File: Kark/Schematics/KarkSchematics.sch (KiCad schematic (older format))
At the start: 29 parts

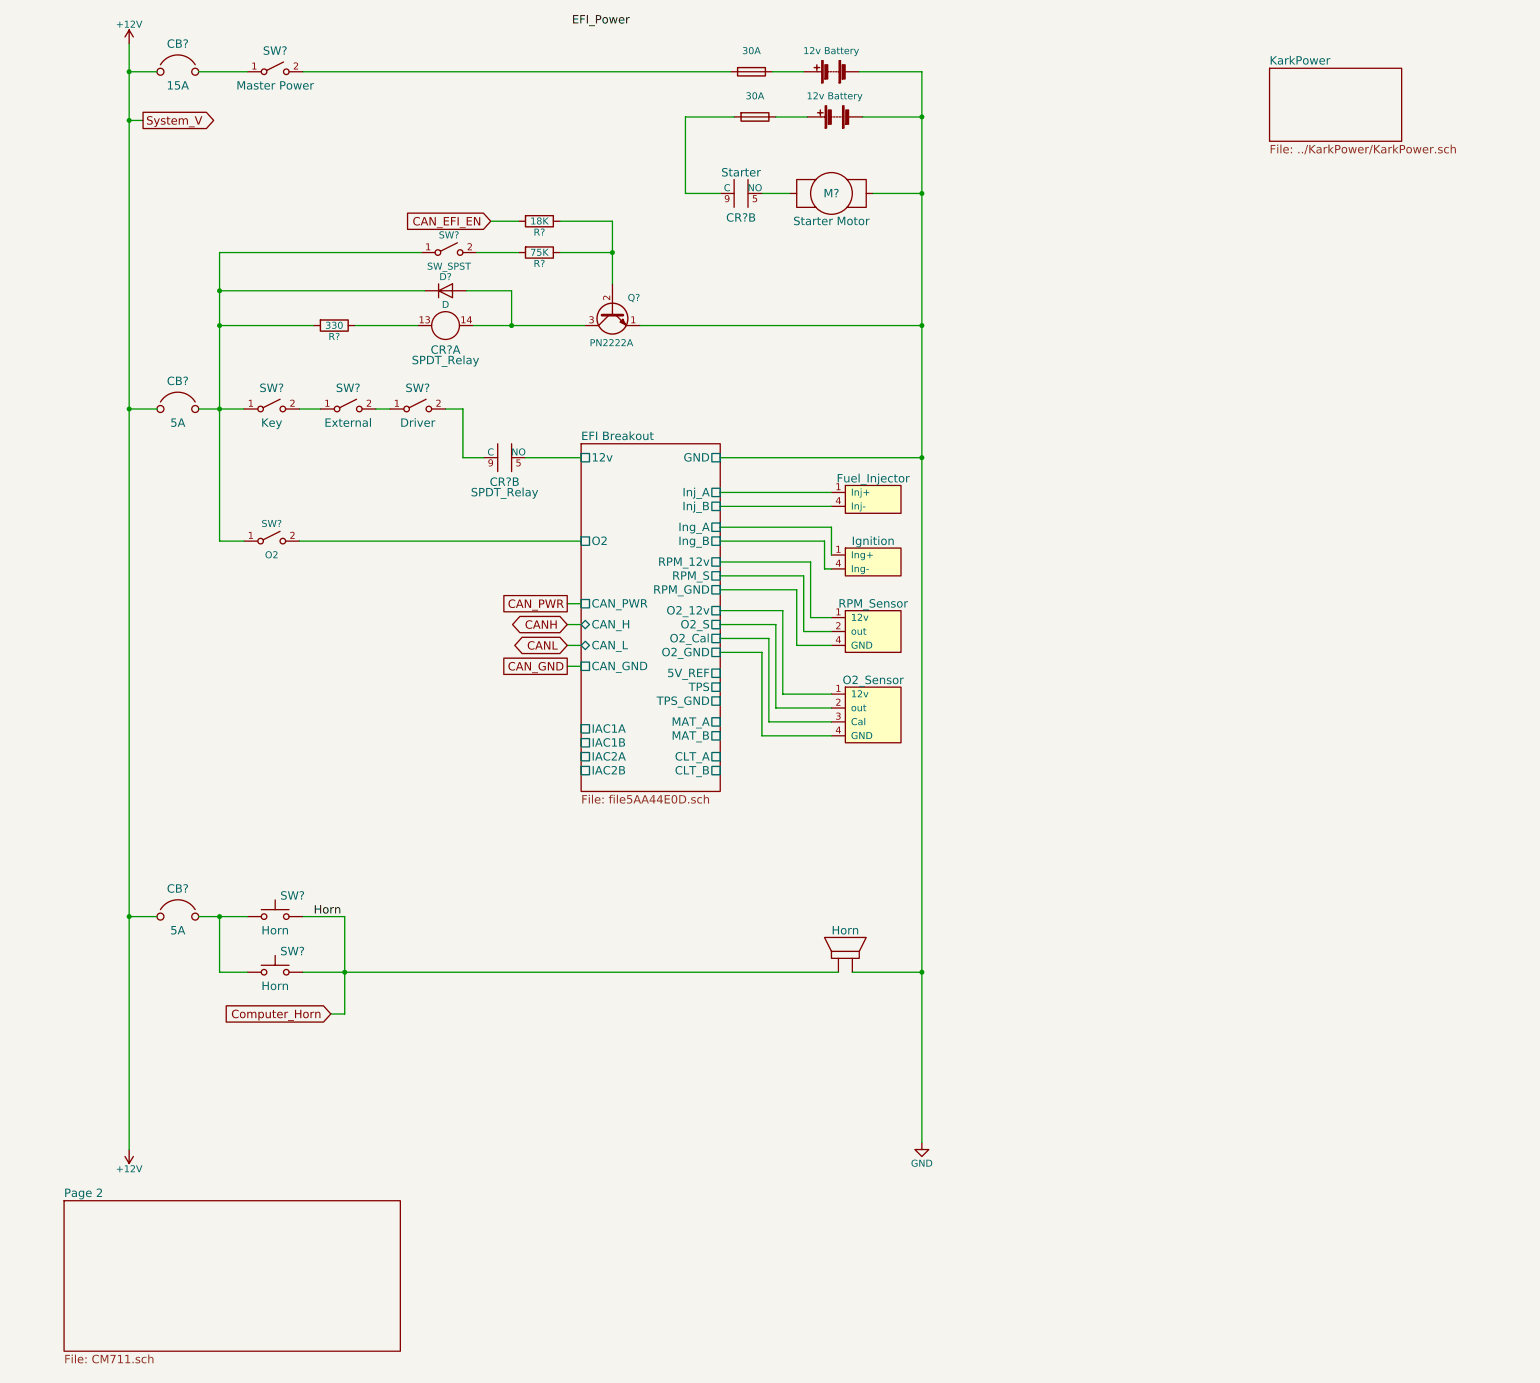
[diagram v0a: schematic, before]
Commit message: Added Starter and Fuel pump
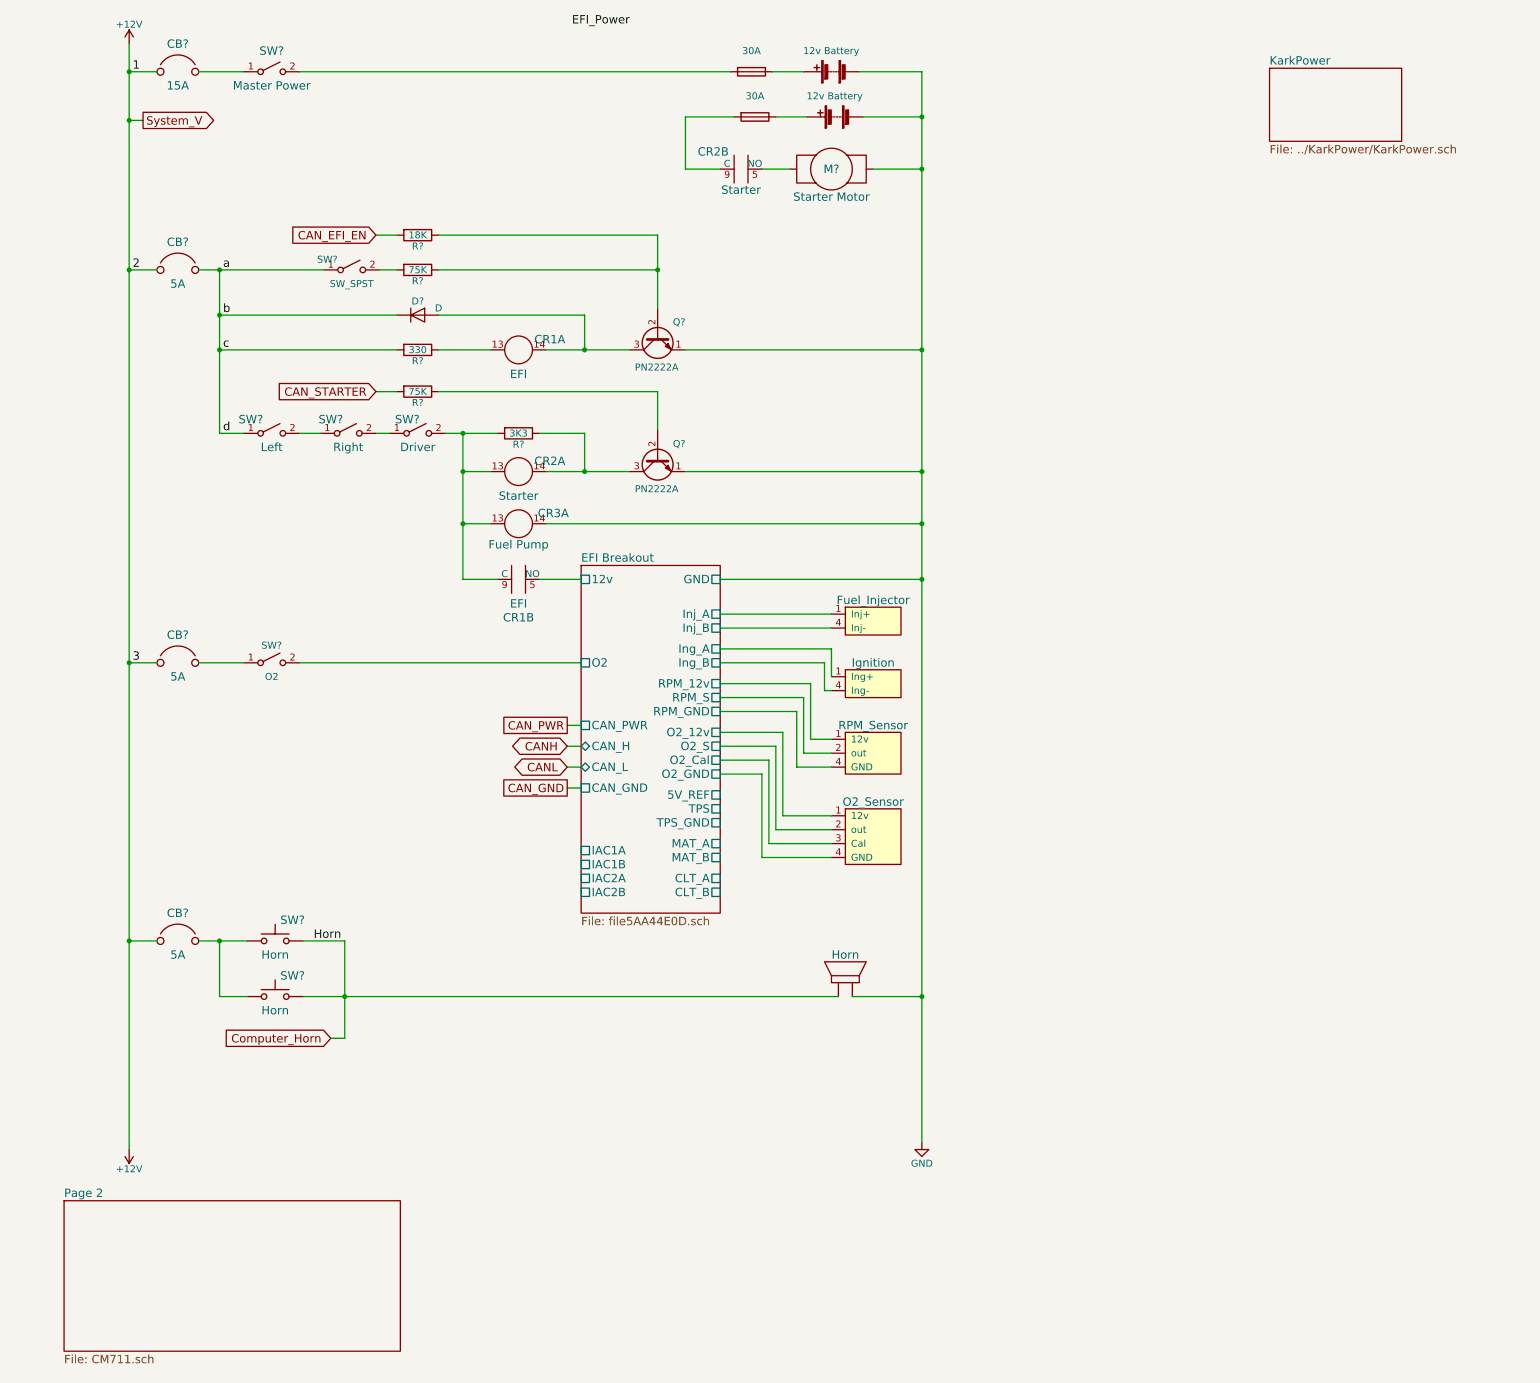
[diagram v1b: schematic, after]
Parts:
- added CB?: 5A, symbol CB
- added unit 1 of CR2
- added CR3: Fuel Pump, symbol SPDT_Relay
- added Q?: PN2222A, TO_SOT_Packages_THT:TO-92_Inline_Wide, symbol PN2222A
- added R?: 75K, Resistors_THT:R_Axial_DIN0207_L6.3mm_D2.5mm_P7.62mm_Horizontal, symbol R
- added R?: 3K3, Resistors_THT:R_Axial_DIN0207_L6.3mm_D2.5mm_P7.62mm_Horizontal, symbol R
- CR1: renamed from CR?; value SPDT_Relay -> EFI
- SW?: value Key -> Left
- SW?: value External -> Right
- gave numbers to parts that had none: 1
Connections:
- net +12V: now also CB?.1 (Line)
- net GND: now also CR3.14, Q?.1 (E)
- net a: now reaches CB?.2 (Load), D?.1 (K), R?.2, SW?.1 (A), SW?.1 (A)
- net a: no longer SW?.1 (A)
- net at CR1.9 (C), SW?.2 (B): now also CR2.13, CR3.13, R?.2
- new net: CB?.2 (Load), SW?.1 (A)
- new net: Q?.2 (B), R?.1
- new net: CR2.14, Q?.3 (C), R?.1
- new net CAN_STARTER: R?.2
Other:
- moved on the sheet: CB?, CR1A, CR1B, CR2B, D?, M?, Q?, R?, SW?

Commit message: Schematic corrections
Corrected wiring for fuel pump and moved the EFI chip over to accomodate the change
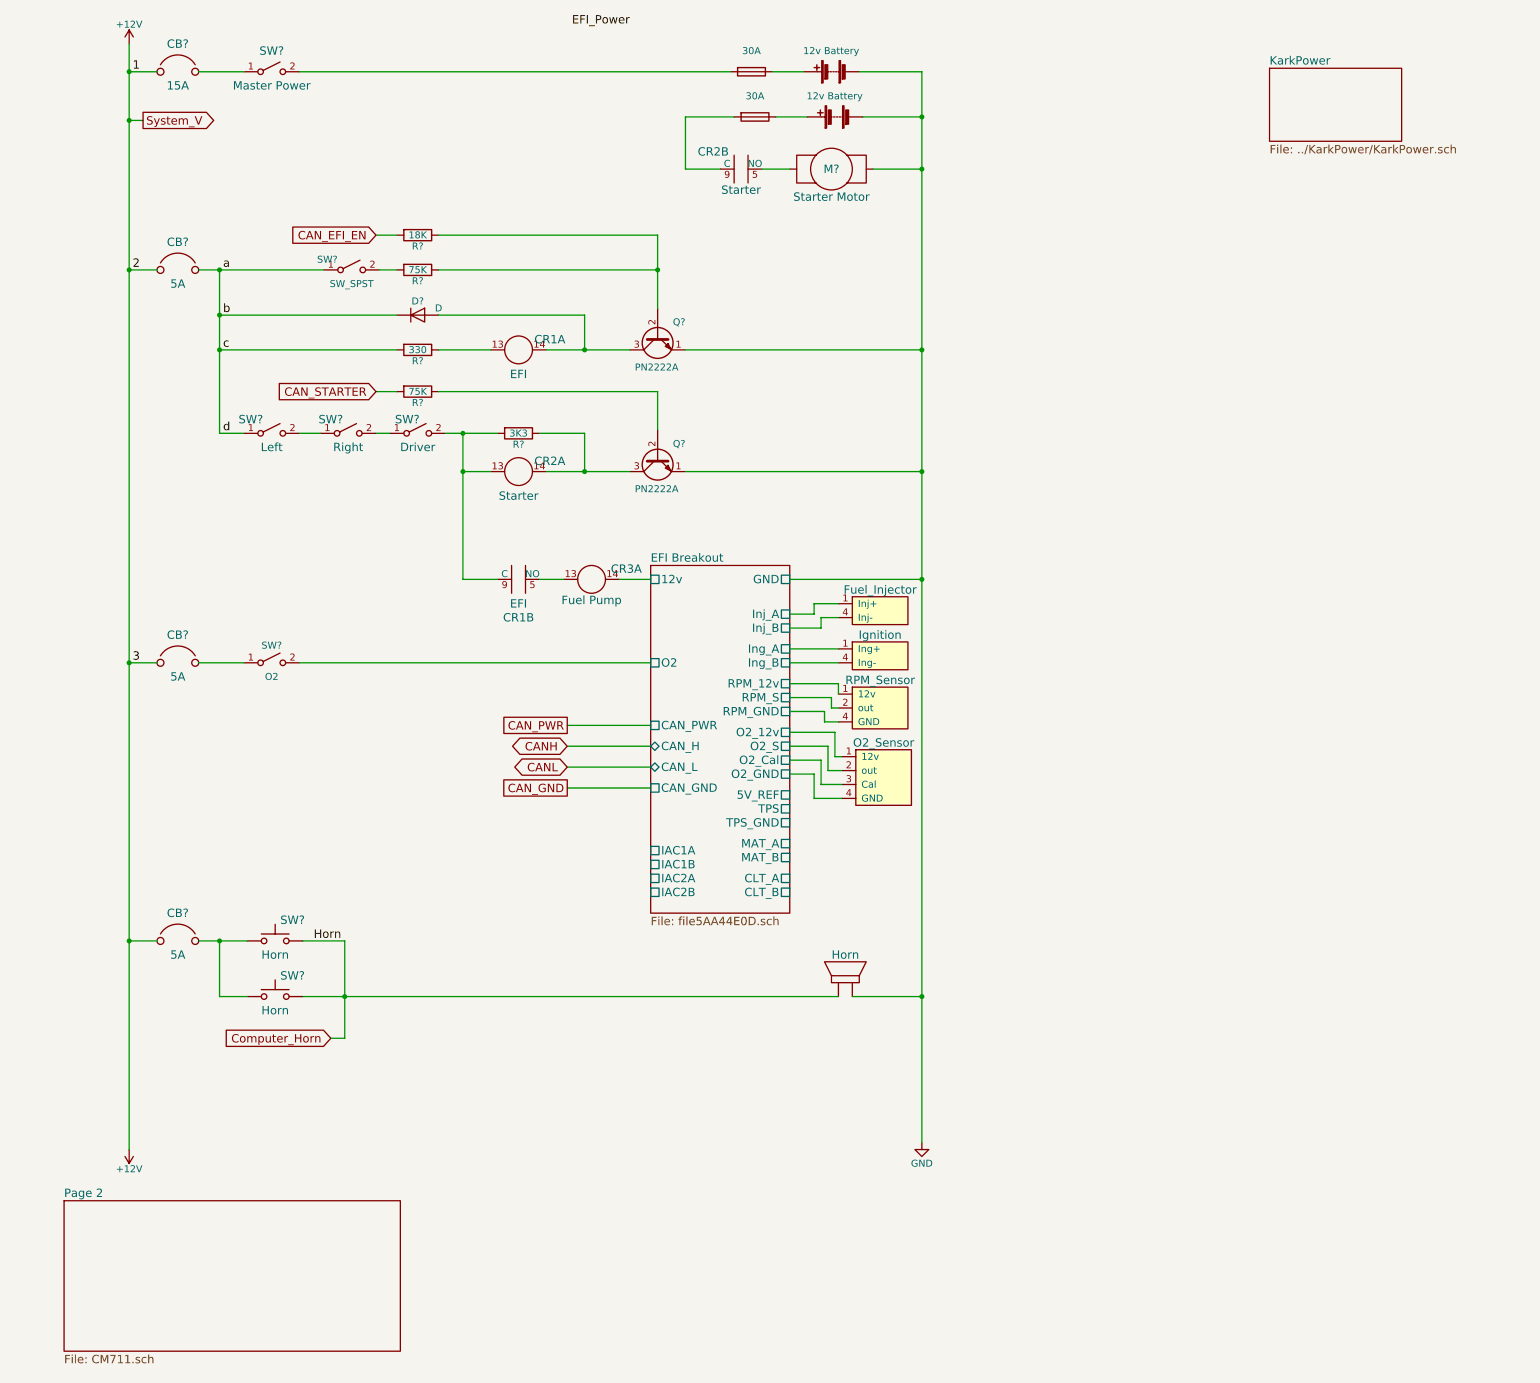
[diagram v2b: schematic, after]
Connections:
- net EFI Breakout/12v: now also CR3.14; no longer CR1.5 (NO)
- net GND: no longer CR3.14
- net at CR1.9 (C), CR2.13, R?.2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: no longer CR3.13
- new net: CR1.5 (NO), CR3.13
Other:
- moved on the sheet: CR3A

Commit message: Kark Schematic additions
Fixed fuel pump
Added wheel sheetand digital switches
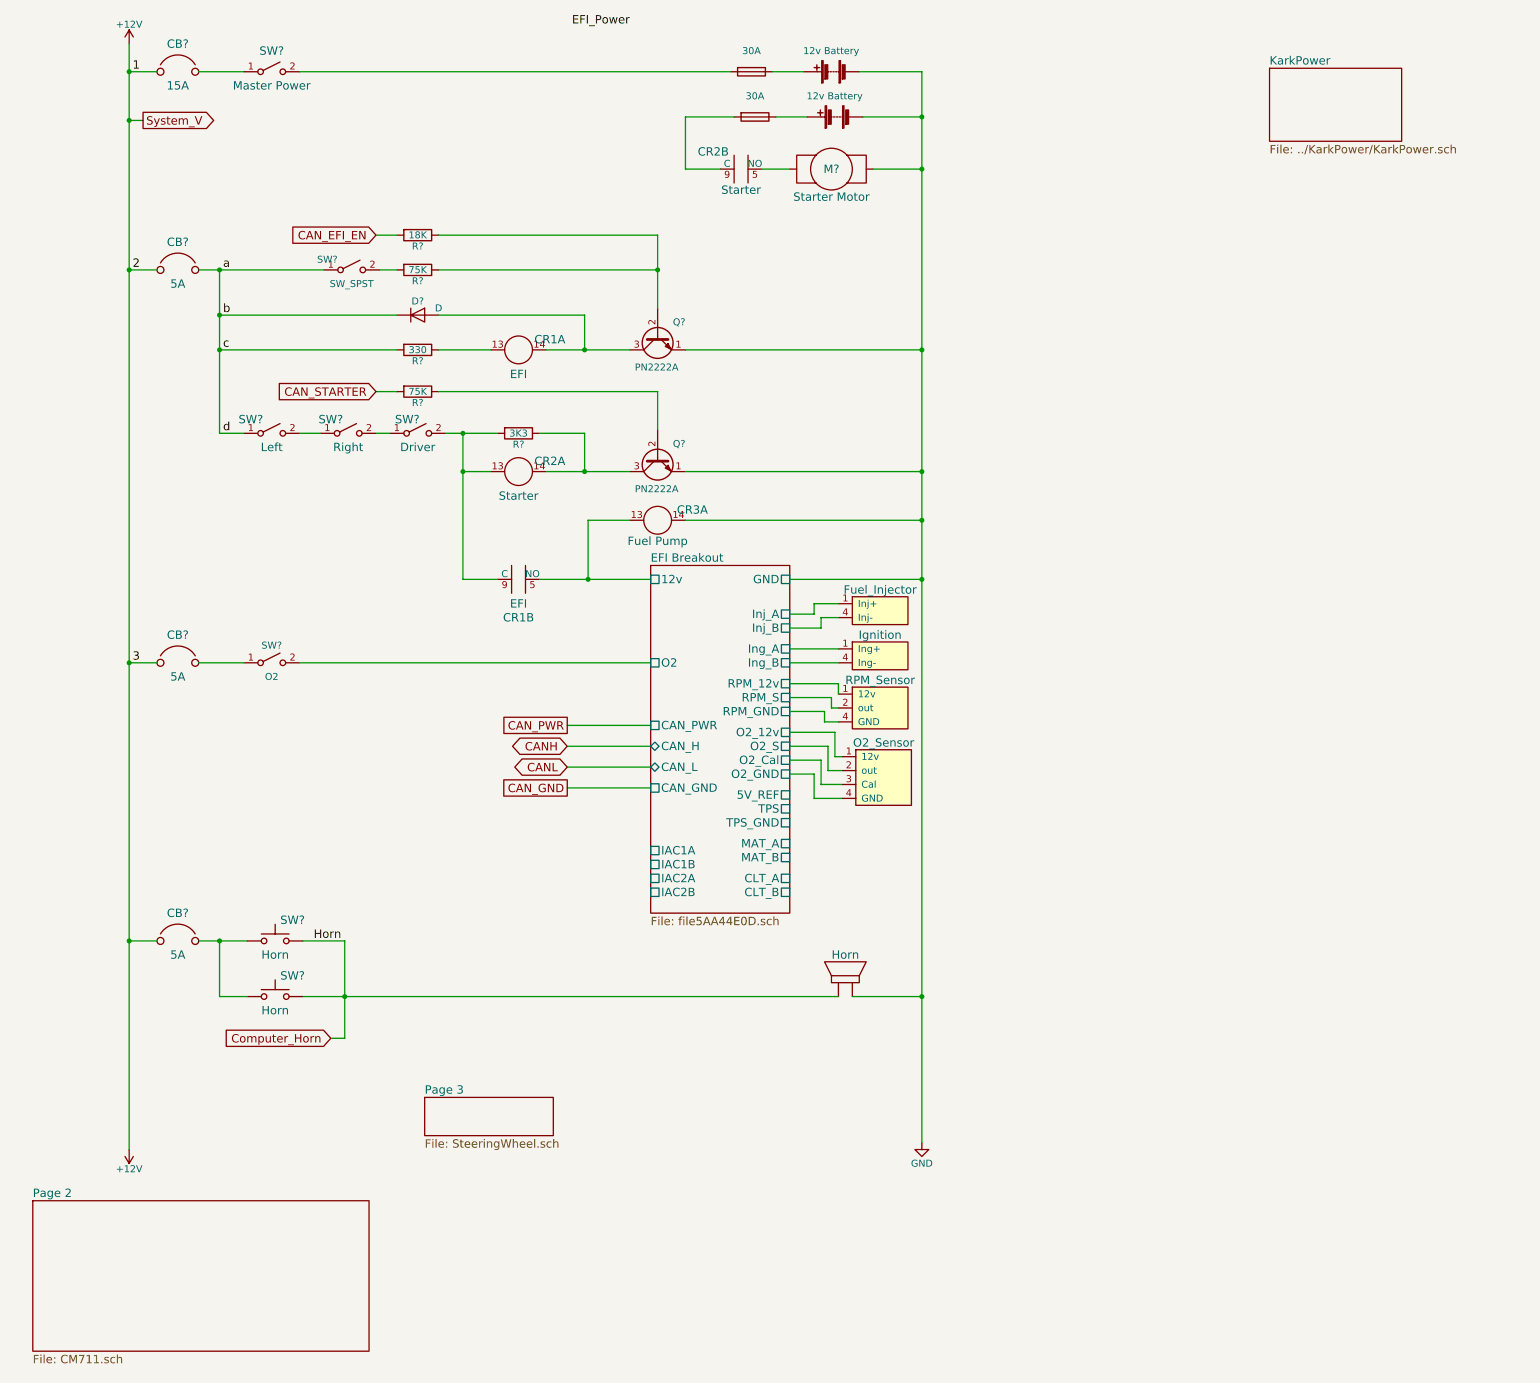
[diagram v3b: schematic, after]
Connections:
- net EFI Breakout/12v: now also CR1.5 (NO), CR3.13; no longer CR3.14
- net GND: now also CR3.14
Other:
- moved on the sheet: CR3A
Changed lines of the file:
@@
 $Descr USLetter 8500 11000 portrait
 encoding utf-8
-Sheet 1 4
+Sheet 1 5
 Title "Kark - Gasoline Prototype"
 Date "2018-03-10"
@@
 $EndComp
 $Sheet
-S 1032 9218 2418 1082
+S 807  9218 2418 1082
 U 5AA44E13
 F0 "Page 2" 60
@@
 Connection ~ 1500 2525
 Wire Wire Line
-	2150 2525 2150 3700
+	2150 2525 2150 2850
+Wire Wire Line
+	2150 2850 2150 3100
+Wire Wire Line
+	2150 3100 2150 3700
 Wire Wire Line
 	2750 7350 3050 7350
 Wire Wire Line
-	3050 7350 3050 8050
+	3050 7350 3050 7750
+Wire Wire Line
+	3050 7750 3050 8050
 Connection ~ 3050 7750
 Wire Wire Line
@@
 	6250 5350 6600 5350
 Wire Wire Line
-	2750 7750 6600 7750
+	2750 7750 3050 7750
+Wire Wire Line
+	3050 7750 6600 7750
 Wire Wire Line
 	7200 7750 6700 7750
 Wire Wire Line
-	7200 1100 7200 8800
+	7200 1100 7200 1425
+Wire Wire Line
+	7200 1425 7200 1800
+Wire Wire Line
+	7200 1800 7200 3100
+Wire Wire Line
+	7200 3100 7200 3975
+Wire Wire Line
+	7200 3975 7200 4325
+Wire Wire Line
+	7200 4325 7200 4750
+Wire Wire Line
+	7200 4750 7200 7750
+Wire Wire Line
+	7200 7750 7200 8800
 Wire Wire Line
 	5500 1800 5750 1800
@@
 Connection ~ 7200 1800
 Wire Wire Line
-	1500 900  1500 8850
+	1500 900  1500 1100
+Wire Wire Line
+	1500 1100 1500 1450
+Wire Wire Line
+	1500 1450 1500 2525
+Wire Wire Line
+	1500 2525 1500 5350
+Wire Wire Line
+	1500 5350 1500 7350
+Wire Wire Line
+	1500 7350 1500 8850
 Wire Wire Line
 	3050 8050 2950 8050
@@
 Connection ~ 1500 1450
 Wire Wire Line
-	3775 3700 4150 3700
+	3775 3700 3900 3700
+Wire Wire Line
+	3900 3700 4150 3700
 Wire Wire Line
 	3900 4750 4150 4750
@@
 	3425 3100 2150 3100
 Wire Wire Line
-	4500 3100 5100 3100
+	4500 3100 4775 3100
+Wire Wire Line
+	4775 3100 5100 3100
 Wire Wire Line
 	7200 3100 5500 3100
@@
 Connection ~ 4775 3100
 Wire Wire Line
-	2000 2525 2900 2525
+	2000 2525 2150 2525
+Wire Wire Line
+	2150 2525 2900 2525
 Wire Wire Line
 	3425 2525 3300 2525
@@
 	3725 2525 5300 2525
 Wire Wire Line
-	5300 2275 5300 2800
+	5300 2275 5300 2525
+Wire Wire Line
+	5300 2525 5300 2800
 Connection ~ 5300 2525
 Wire Wire Line
@@
 	2000 5350 2325 5350
 Wire Wire Line
-	2000 7350 2350 7350
+	2000 7350 2150 7350
+Wire Wire Line
+	2150 7350 2350 7350
 Wire Wire Line
 	1700 7350 1500 7350
@@
 $EndComp
 Wire Wire Line
-	4500 3975 5100 3975
+	4500 3975 4775 3975
+Wire Wire Line
+	4775 3975 5100 3975
 Text GLabel 3275 3400 0    60   Input ~ 0
 CAN_STARTER
@@
 L SPDT_Relay CR3
 U 1 1 5AB72A85
-P 4825 4750
-F 0 "CR3" H 5075 4825 60  0000 C CNN
-F 1 "Fuel Pump" H 4825 4600 60  0000 C CNN
-F 2 "" H 4825 4750 60  0000 C CNN
-F 3 "" H 4825 4750 60  0000 C CNN
-	1    4825 4750
+P 5300 4325
+F 0 "CR3" H 5550 4400 60  0000 C CNN
+F 1 "Fuel Pump" H 5300 4175 60  0000 C CNN
+F 2 "" H 5300 4325 60  0000 C CNN
+F 3 "" H 5300 4325 60  0000 C CNN
+	1    5300 4325
 	1    0    0    -1
 $EndComp
@@
 	4100 3975 3900 3975
 Wire Wire Line
-	3900 3700 3900 4750
+	3900 3700 3900 3975
+Wire Wire Line
+	3900 3975 3900 4750
 Connection ~ 3900 3975
 Connection ~ 3900 3700
@@
 	6600 5250 6250 5250
 Wire Wire Line
-	5250 4750 5025 4750
-Wire Wire Line
-	4625 4750 4450 4750
+	4450 4750 4800 4750
+Wire Wire Line
+	4800 4750 5250 4750
+Wire Wire Line
+	4800 4750 4800 4325
+Wire Wire Line
+	4800 4325 5100 4325
+Wire Wire Line
+	5500 4325 7200 4325
+Connection ~ 7200 4325
+Connection ~ 4800 4750
+$Sheet
+S 3625 8475 925  275
+U 5AB711C0
+F0 "Page 3" 60
+F1 "SteeringWheel.sch" 60
+$EndSheet
 $EndSCHEMATC

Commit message: Merge with Tinkea's stuff
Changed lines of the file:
@@
 $Descr USLetter 8500 11000 portrait
 encoding utf-8
-Sheet 1 5
+Sheet 1 6
 Title "Kark - Gasoline Prototype"
 Date "2018-03-10"
@@
 	1    0    0    -1
 $EndComp
-$Sheet
-S 807  9218 2418 1082
-U 5AA44E13
-F0 "Page 2" 60
-F1 "CM711.sch" 60
-$EndSheet
 Text GLabel 2950 8050 0    60   Input ~ 0
 Computer_Horn
@@
 Connection ~ 4800 4750
 $Sheet
-S 3625 8475 925  275
-U 5AB711C0
-F0 "Page 3" 60
-F1 "SteeringWheel.sch" 60
+S 650  9125 2800 1200
+U 5AB66DFC
+F0 "Page 2" 60
+F1 "Page2.sch" 60
 $EndSheet
 $EndSCHEMATC
